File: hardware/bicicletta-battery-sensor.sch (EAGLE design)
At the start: 14 parts

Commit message: Nearly finalized PCB for battery sensor module
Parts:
- renumbered U$5 to IC1, U1 to IC2
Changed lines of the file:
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@@
 <part name="R2" library="rcl" deviceset="R-US_" device="R0603" value="1K 1%"/>
 <part name="GND4" library="SparkFun-Aesthetics" deviceset="GND" device=""/>
-<part name="U$5" library="Railstars" deviceset="LMP92064" device=""/>
+<part name="IC1" library="Railstars" deviceset="LMP92064" device=""/>
 <part name="GND1" library="SparkFun-Aesthetics" deviceset="GND" device=""/>
 <part name="C_REFC" library="rcl" deviceset="C-US" device="C0603" value="1uF"/>
@@
 <part name="R4" library="rcl" deviceset="R-US_" device="R0603" value="100"/>
 <part name="C1" library="rcl" deviceset="C-US" device="C0603" value="1nF"/>
-<part name="U1" library="adafruit" deviceset="TXB0104PWR" device=""/>
+<part name="IC2" library="adafruit" deviceset="TXB0104PWR" device=""/>
 <part name="GND7" library="SparkFun-Aesthetics" deviceset="GND" device=""/>
 <part name="P+2" library="SparkFun-Aesthetics" deviceset="3.3V" device=""/>
@@
 <instance part="R2" gate="G$1" x="58.42" y="139.7" rot="R90"/>
 <instance part="GND4" gate="1" x="109.22" y="99.06"/>
-<instance part="U$5" gate="G$1" x="106.68" y="129.54"/>
+<instance part="IC1" gate="G$1" x="106.68" y="129.54"/>
 <instance part="GND1" gate="1" x="134.62" y="116.84"/>
 <instance part="C_REFC" gate="G$1" x="5.08" y="127"/>
@@
 <instance part="R4" gate="G$1" x="68.58" y="114.3"/>
 <instance part="C1" gate="G$1" x="76.2" y="119.38"/>
-<instance part="U1" gate="G$1" x="226.06" y="129.54"/>
+<instance part="IC2" gate="G$1" x="226.06" y="129.54"/>
 <instance part="GND7" gate="1" x="226.06" y="106.68"/>
 <instance part="P+2" gate="G$1" x="223.52" y="152.4"/>
@@
 </segment>
 <segment>
-<pinref part="U1" gate="G$1" pin="A1"/>
+<pinref part="IC2" gate="G$1" pin="A1"/>
 <wire x1="210.82" y1="132.08" x2="193.04" y2="132.08" width="0.1524" layer="91"/>
 <label x="193.04" y="132.08" size="1.778" layer="95"/>
@@
 </segment>
 <segment>
-<pinref part="U1" gate="G$1" pin="A2"/>
+<pinref part="IC2" gate="G$1" pin="A2"/>
 <wire x1="210.82" y1="129.54" x2="193.04" y2="129.54" width="0.1524" layer="91"/>
 <label x="193.04" y="129.54" size="1.778" layer="95"/>
@@
 </segment>
 <segment>
-<pinref part="U1" gate="G$1" pin="A3"/>
+<pinref part="IC2" gate="G$1" pin="A3"/>
 <wire x1="210.82" y1="127" x2="193.04" y2="127" width="0.1524" layer="91"/>
 <label x="193.04" y="127" size="1.778" layer="95"/>
@@
 </segment>
 <segment>
-<pinref part="U1" gate="G$1" pin="A4"/>
+<pinref part="IC2" gate="G$1" pin="A4"/>
 <wire x1="210.82" y1="124.46" x2="193.04" y2="124.46" width="0.1524" layer="91"/>
 <label x="193.04" y="124.46" size="1.778" layer="95"/>
@@
 <pinref part="R2" gate="G$1" pin="1"/>
 <pinref part="GND5" gate="1" pin="GND"/>
-<pinref part="U$5" gate="G$1" pin="INVG"/>
+<pinref part="IC1" gate="G$1" pin="INVG"/>
 <wire x1="88.9" y1="132.08" x2="63.5" y2="132.08" width="0.1524" layer="91"/>
 <wire x1="63.5" y1="132.08" x2="63.5" y2="134.62" width="0.1524" layer="91"/>
@@
 </segment>
 <segment>
-<pinref part="U$5" gate="G$1" pin="RESET"/>
+<pinref part="IC1" gate="G$1" pin="RESET"/>
 <wire x1="132.08" y1="124.46" x2="134.62" y2="124.46" width="0.1524" layer="91"/>
 <wire x1="134.62" y1="124.46" x2="134.62" y2="119.38" width="0.1524" layer="91"/>
@@
 </segment>
 <segment>
-<pinref part="U$5" gate="G$1" pin="GND"/>
+<pinref part="IC1" gate="G$1" pin="GND"/>
 <wire x1="109.22" y1="111.76" x2="109.22" y2="104.14" width="0.1524" layer="91"/>
-<pinref part="U$5" gate="G$1" pin="DGND"/>
+<pinref part="IC1" gate="G$1" pin="DGND"/>
 <wire x1="114.3" y1="111.76" x2="114.3" y2="104.14" width="0.1524" layer="91"/>
 <wire x1="114.3" y1="104.14" x2="109.22" y2="104.14" width="0.1524" layer="91"/>
-<pinref part="U$5" gate="G$1" pin="REFG"/>
+<pinref part="IC1" gate="G$1" pin="REFG"/>
 <wire x1="104.14" y1="111.76" x2="104.14" y2="104.14" width="0.1524" layer="91"/>
 <wire x1="104.14" y1="104.14" x2="109.22" y2="104.14" width="0.1524" layer="91"/>
@@
 </segment>
 <segment>
-<pinref part="U1" gate="G$1" pin="GND"/>
+<pinref part="IC2" gate="G$1" pin="GND"/>
 <wire x1="226.06" y1="114.3" x2="226.06" y2="109.22" width="0.1524" layer="91"/>
 <pinref part="GND7" gate="1" pin="GND"/>
@@
 </segment>
 <segment>
-<pinref part="U$5" gate="G$1" pin="VDD"/>
+<pinref part="IC1" gate="G$1" pin="VDD"/>
 <wire x1="109.22" y1="147.32" x2="109.22" y2="152.4" width="0.1524" layer="91"/>
 <pinref part="U$3" gate="G$1" pin="5V"/>
 <wire x1="109.22" y1="152.4" x2="111.76" y2="152.4" width="0.1524" layer="91"/>
-<pinref part="U$5" gate="G$1" pin="VDIG"/>
+<pinref part="IC1" gate="G$1" pin="VDIG"/>
 <wire x1="114.3" y1="147.32" x2="114.3" y2="152.4" width="0.1524" layer="91"/>
 <wire x1="114.3" y1="152.4" x2="111.76" y2="152.4" width="0.1524" layer="91"/>
@@
 </segment>
 <segment>
-<pinref part="U1" gate="G$1" pin="VCCB"/>
+<pinref part="IC2" gate="G$1" pin="VCCB"/>
 <wire x1="228.6" y1="147.32" x2="228.6" y2="149.86" width="0.1524" layer="91"/>
 <pinref part="U$9" gate="G$1" pin="5V"/>
@@
 </segment>
 <segment>
-<pinref part="U1" gate="G$1" pin="VCCA"/>
+<pinref part="IC2" gate="G$1" pin="VCCA"/>
 <wire x1="223.52" y1="147.32" x2="223.52" y2="149.86" width="0.1524" layer="91"/>
 <pinref part="P+2" gate="G$1" pin="3.3V"/>
-<pinref part="U1" gate="G$1" pin="OE"/>
+<pinref part="IC2" gate="G$1" pin="OE"/>
 <wire x1="223.52" y1="149.86" x2="223.52" y2="152.4" width="0.1524" layer="91"/>
 <wire x1="210.82" y1="137.16" x2="208.28" y2="137.16" width="0.1524" layer="91"/>
@@
 <wire x1="66.04" y1="144.78" x2="66.04" y2="134.62" width="0.1524" layer="91"/>
 <wire x1="66.04" y1="134.62" x2="88.9" y2="134.62" width="0.1524" layer="91"/>
-<pinref part="U$5" gate="G$1" pin="INVP"/>
+<pinref part="IC1" gate="G$1" pin="INVP"/>
 <junction x="58.42" y="144.78"/>
 </segment>
@@
 <net name="REFC" class="0">
 <segment>
-<pinref part="U$5" gate="G$1" pin="REFC"/>
+<pinref part="IC1" gate="G$1" pin="REFC"/>
 <wire x1="104.14" y1="147.32" x2="104.14" y2="152.4" width="0.1524" layer="91"/>
 <label x="104.14" y="149.86" size="1.778" layer="95" rot="R90"/>
@@
 <wire x1="76.2" y1="121.92" x2="78.74" y2="121.92" width="0.1524" layer="91"/>
 <wire x1="78.74" y1="121.92" x2="78.74" y2="127" width="0.1524" layer="91"/>
-<pinref part="U$5" gate="G$1" pin="INCP"/>
+<pinref part="IC1" gate="G$1" pin="INCP"/>
 <wire x1="78.74" y1="127" x2="88.9" y2="127" width="0.1524" layer="91"/>
 <junction x="76.2" y="121.92"/>
@@
 <net name="N$4" class="0">
 <segment>
-<pinref part="U$5" gate="G$1" pin="INCN"/>
+<pinref part="IC1" gate="G$1" pin="INCN"/>
 <wire x1="88.9" y1="124.46" x2="83.82" y2="124.46" width="0.1524" layer="91"/>
 <wire x1="83.82" y1="124.46" x2="83.82" y2="114.3" width="0.1524" layer="91"/>
@@
 <net name="SS_5" class="0">
 <segment>
-<pinref part="U$5" gate="G$1" pin="CSB"/>
+<pinref part="IC1" gate="G$1" pin="CSB"/>
 <wire x1="132.08" y1="134.62" x2="149.86" y2="134.62" width="0.1524" layer="91"/>
 <label x="139.7" y="134.62" size="1.778" layer="95"/>
 </segment>
 <segment>
-<pinref part="U1" gate="G$1" pin="B4"/>
+<pinref part="IC2" gate="G$1" pin="B4"/>
 <wire x1="241.3" y1="124.46" x2="264.16" y2="124.46" width="0.1524" layer="91"/>
 <label x="256.54" y="124.46" size="1.778" layer="95"/>
@@
 <net name="CLK_5" class="0">
 <segment>
-<pinref part="U$5" gate="G$1" pin="SCLK"/>
+<pinref part="IC1" gate="G$1" pin="SCLK"/>
 <wire x1="132.08" y1="132.08" x2="149.86" y2="132.08" width="0.1524" layer="91"/>
 <label x="139.7" y="132.08" size="1.778" layer="95"/>
 </segment>
 <segment>
-<pinref part="U1" gate="G$1" pin="B3"/>
+<pinref part="IC2" gate="G$1" pin="B3"/>
 <wire x1="241.3" y1="127" x2="264.16" y2="127" width="0.1524" layer="91"/>
 <label x="256.54" y="127" size="1.778" layer="95"/>
@@
 <net name="MOSI_5" class="0">
 <segment>
-<pinref part="U$5" gate="G$1" pin="SDI"/>
+<pinref part="IC1" gate="G$1" pin="SDI"/>
 <wire x1="132.08" y1="129.54" x2="149.86" y2="129.54" width="0.1524" layer="91"/>
 <label x="139.7" y="129.54" size="1.778" layer="95"/>
 </segment>
 <segment>
-<pinref part="U1" gate="G$1" pin="B2"/>
+<pinref part="IC2" gate="G$1" pin="B2"/>
 <wire x1="241.3" y1="129.54" x2="264.16" y2="129.54" width="0.1524" layer="91"/>
 <label x="256.54" y="129.54" size="1.778" layer="95"/>
@@
 <net name="MISO_5" class="0">
 <segment>
-<pinref part="U$5" gate="G$1" pin="SDO"/>
+<pinref part="IC1" gate="G$1" pin="SDO"/>
 <wire x1="132.08" y1="127" x2="149.86" y2="127" width="0.1524" layer="91"/>
 <label x="139.7" y="127" size="1.778" layer="95"/>
 </segment>
 <segment>
-<pinref part="U1" gate="G$1" pin="B1"/>
+<pinref part="IC2" gate="G$1" pin="B1"/>
 <wire x1="241.3" y1="132.08" x2="264.16" y2="132.08" width="0.1524" layer="91"/>
 <label x="256.54" y="132.08" size="1.778" layer="95"/>

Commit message: Add value to the TXB0108
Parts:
- IC2: value (none) -> TXB0108
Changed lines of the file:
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@@
 <part name="R4" library="rcl" deviceset="R-US_" device="R0603" value="100"/>
 <part name="C1" library="rcl" deviceset="C-US" device="C0603" value="1nF"/>
-<part name="IC2" library="adafruit" deviceset="TXB0104PWR" device=""/>
+<part name="IC2" library="adafruit" deviceset="TXB0104PWR" device="" value="TXB0108"/>
 <part name="GND7" library="SparkFun-Aesthetics" deviceset="GND" device=""/>
 <part name="P+2" library="SparkFun-Aesthetics" deviceset="3.3V" device=""/>

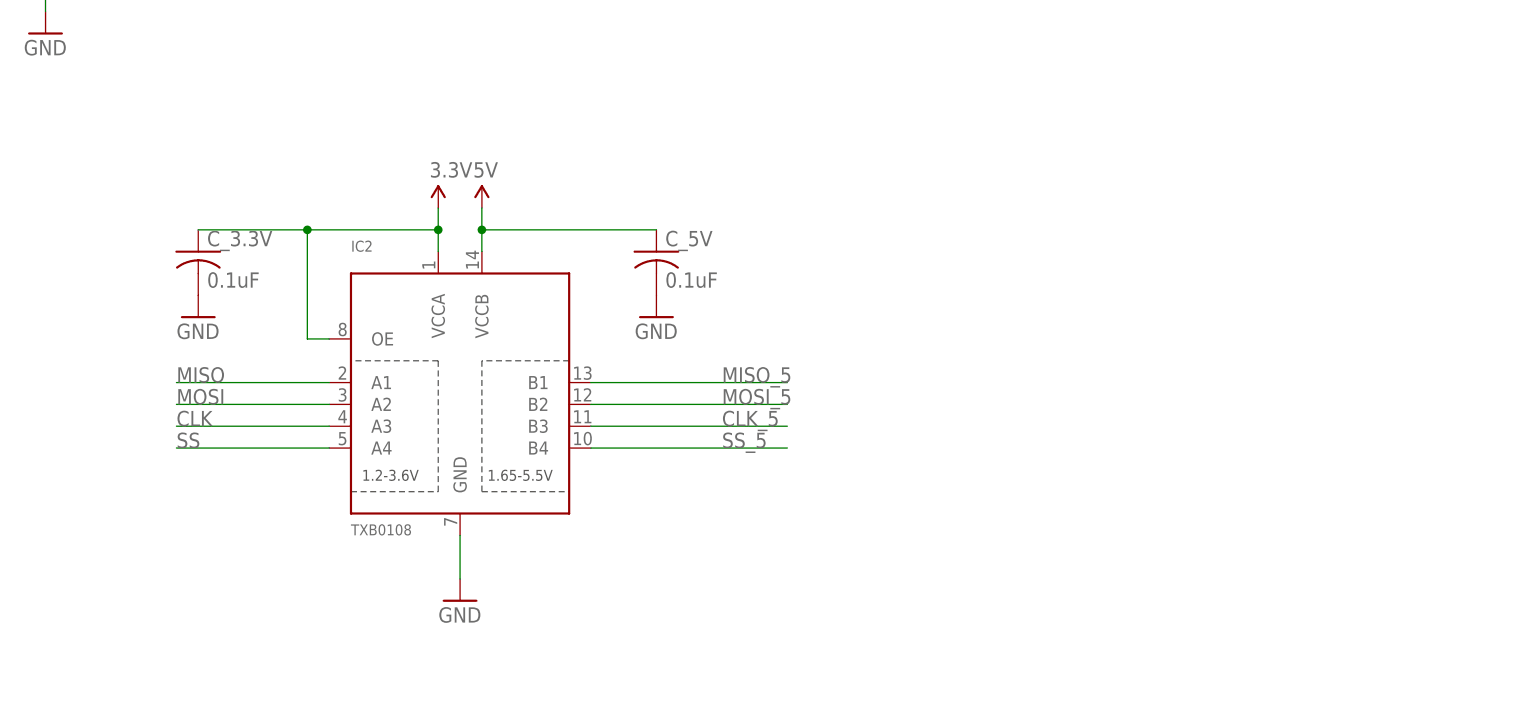
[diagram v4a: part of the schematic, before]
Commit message: Trying out a new level shifter, as the previous integrated one proved awfully fiddly in practice.
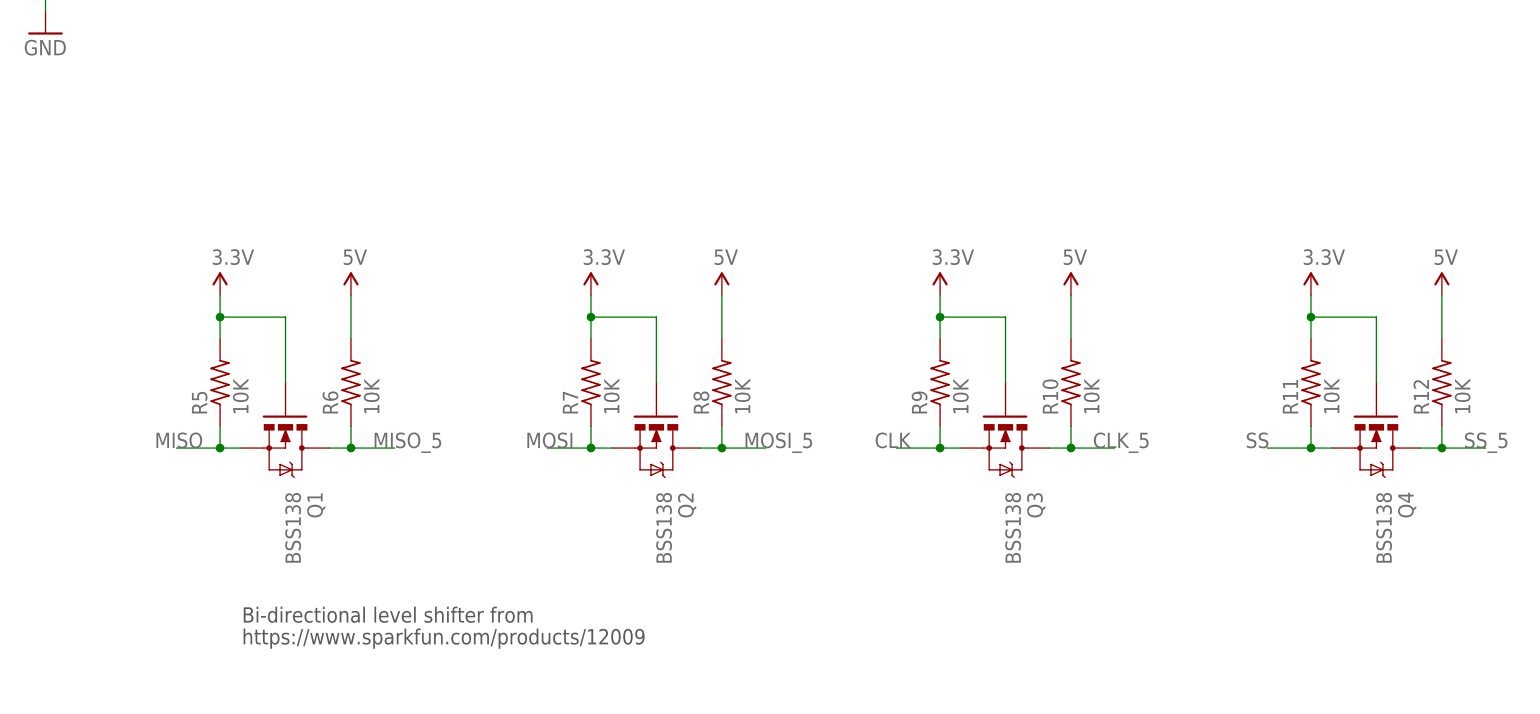
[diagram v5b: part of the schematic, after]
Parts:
- removed C_3.3V, C_5V: 0.1uF, rcl:C-USC0603
- removed IC2: TXB0108, adafruit:TXB0104PWR
- added Q1, Q2, Q3, Q4: BSS138, SparkFun-DiscreteSemi:MOSFET-NCHANNELBSS138
- added R10, R11, R12, R5, R6, R7, R8, R9: 10K, rcl:R-US_R0603
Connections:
- net 3.3V: now also Q1.G, Q2.G, Q3.G, Q4.G, R11.2, R5.2, R7.2, R9.2; no longer C_3.3V.1, IC2.OE, IC2.VCCA
- net 5V: now also R10.2, R12.2, R6.2, R8.2; no longer C_5V.1, IC2.VCCB
- net CLK: now also Q3.S, R9.1; no longer IC2.A3
- net CLK_5: now also Q3.D, R10.1; no longer IC2.B3
- net GND: no longer C_3.3V.2, C_5V.2, IC2.GND
- net MISO: now also Q1.S, R5.1; no longer IC2.A1
- net MISO_5: now also Q1.D, R6.1; no longer IC2.B1
- net MOSI: now also Q2.S, R7.1; no longer IC2.A2
- net MOSI_5: now also Q2.D, R8.1; no longer IC2.B2
- net SS: now also Q4.S, R11.1; no longer IC2.A4
- net SS_5: now also Q4.D, R12.1; no longer IC2.B4
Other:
- note added: "Bi-directional level shifter from"
- note added: "https://www.sparkfun.com/products/12009"
